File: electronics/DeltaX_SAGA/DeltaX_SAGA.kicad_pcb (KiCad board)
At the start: 4 copper layers, 51.2 x 58.9 mm, 68 parts, among them J1 USB_B_Micro, J10 Motor3_Encoder, J11 Motor1_OUT, J12 Motor2_OUT, J13 Motor3_OUT, J14 TestPt1, J15 TestPt2, J16 TestGND, J18 STLink, J2 Programmer, J3 Servo Signal, J4 Servo Power, J5 Power(6-38V), J6 Thrower Signal, J7 Thrower Power, J8 Motor1_Encoder, J9 Motor2_Encoder, U1 CM1223, U10 DRV8243, U11 DRV8243, U2 NCP164C, U3 STM32G441KB, U4 NCV8730, U5 NCP164C, U6 MAX14930, U7 MAX14930, U8 MAX12930, U9 DRV8243

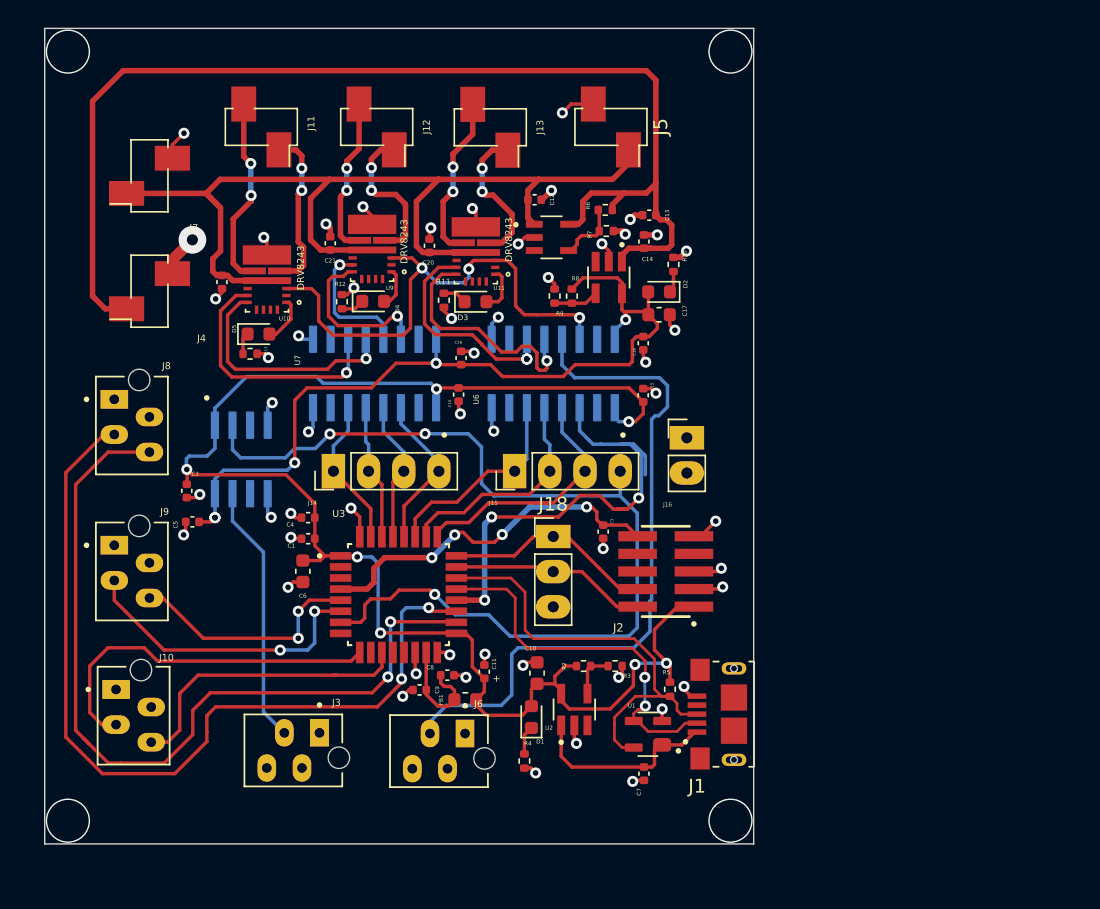
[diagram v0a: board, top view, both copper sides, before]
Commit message: Updated the PCB design
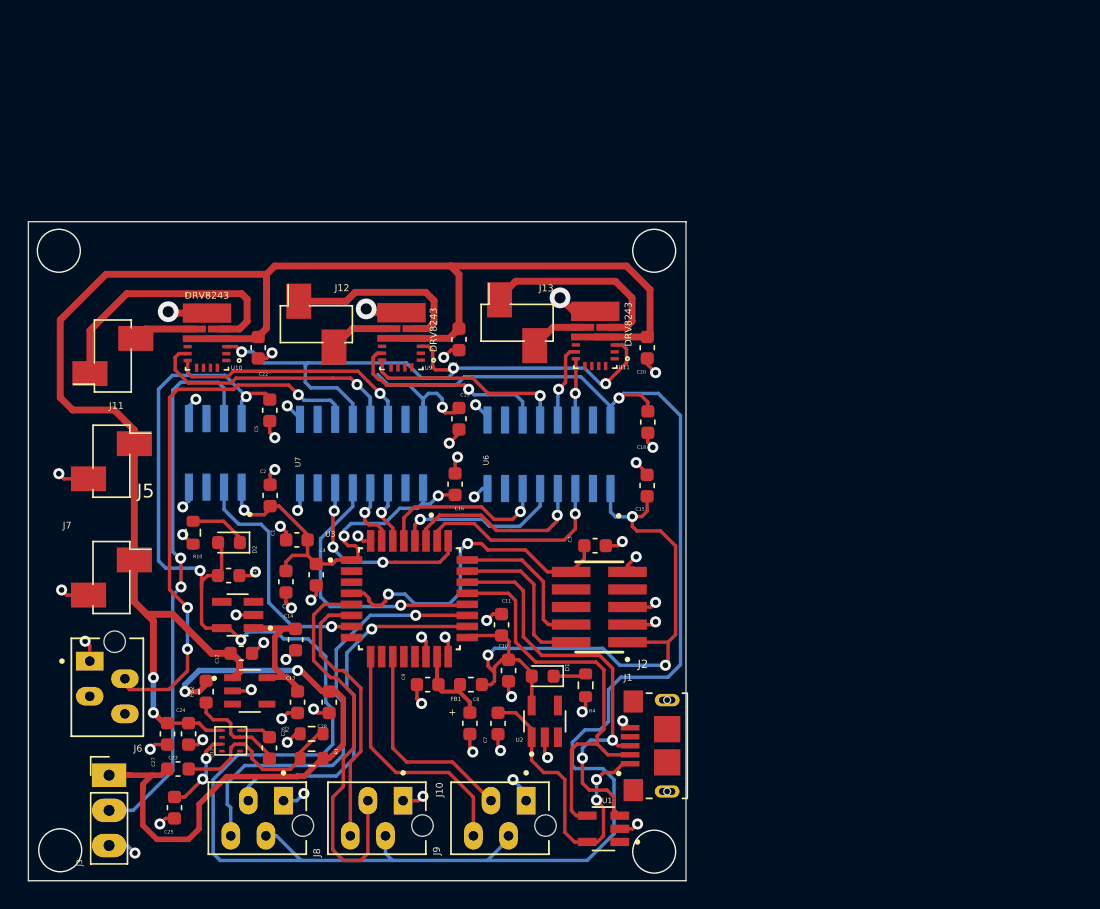
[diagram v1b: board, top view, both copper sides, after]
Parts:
- removed D3, D4, D5: LED, LED_SMD:LED_0603_1608Metric
- removed J14: TestPt1, Connector_PinHeader_2.54mm:PinHeader_1x04_P2.54mm_Vertical
- removed J15: TestPt2, Connector_PinHeader_2.54mm:PinHeader_1x04_P2.54mm_Vertical
- removed J16: TestGND, Connector_PinHeader_2.54mm:PinHeader_1x02_P2.54mm_Vertical
- removed J18: STLink, Connector_PinHeader_2.54mm:PinHeader_1x03_P2.54mm_Vertical
- removed J4: Servo Power, Connector_PinHeader_2.54mm:PinHeader_1x02_P2.54mm_Vertical_SMD_Pin1Right
- removed R11, R12, R13, R5: 1k5, Resistor_SMD:R_0402_1005Metric
- removed R3: 100k, Resistor_SMD:R_0402_1005Metric
- removed R6: 2M4, Resistor_SMD:R_0402_1005Metric
- removed R7: 750k, Resistor_SMD:R_0402_1005Metric
- removed R8: R1, Resistor_SMD:R_0402_1005Metric
- removed R9: R2, Resistor_SMD:R_0402_1005Metric
- added C23: 10uF, Capacitor_SMD:C_0603_1608Metric, F.Cu at (110.7, 123.2)
- added C24: 100nF, Capacitor_SMD:C_0603_1608Metric, F.Cu at (112.3, 123.2)
- added C25: 33nF, Capacitor_SMD:C_0603_1608Metric, F.Cu at (111.3, 128.5)
- added C26: 100nF, Capacitor_SMD:C_0603_1608Metric, F.Cu at (118.1, 124.2)
- added C27: 22pF, Capacitor_SMD:C_0603_1608Metric, F.Cu at (111.5, 125.7)
- added C28: 47uF, Capacitor_SMD:C_0603_1608Metric, F.Cu at (122.4, 120.9)
- added FB2: FerriteBead_Small, Inductor_SMD:L_0603_1608Metric, F.Cu at (113.5, 120.1)
- added R1: 52k3, Resistor_SMD:R_0603_1608Metric, F.Cu at (121.2, 125.0)
- added U12: TPS62932, TPS62933:TPS62933, F.Cu at (114.7, 122.9)
- C1, C11, C12, C13, C14, C15, C16, C18, C19, C2, C3, C4, C5, C7, C8, C9: footprint Capacitor_SMD:C_0402_1005Metric -> Capacitor_SMD:C_0603_1608Metric
- C20, C21, C22: value 0.1uF -> 50uF; footprint Capacitor_SMD:C_0402_1005Metric -> Capacitor_SMD:C_0603_1608Metric
- J3: value Servo Signal -> SERVO; footprint Micro-MaTch215079-4:TE_7-215079-4 -> Connector_PinHeader_2.54mm:PinHeader_1x03_P2.54mm_Vertical
- R10, R4: footprint Resistor_SMD:R_0402_1005Metric -> Resistor_SMD:R_0603_1608Metric
- R2: value 200k -> 10k; footprint Resistor_SMD:R_0402_1005Metric -> Resistor_SMD:R_0603_1608Metric
- U1: footprint CM1223:SOT192P237X122-4N -> CM1223-02SO:SOT95P280X145-5N
- moved J5 43.4 mm to (106.7, 103.5), turned to 0 degrees
- moved C13 43.4 mm to (120.1, 120.9), turned to -90 degrees
- moved R10 39.7 mm to (112.6, 108.7), turned to -90 degrees
- moved U4 39.3 mm to (116.7, 120.1)
- moved C12 39.0 mm to (116.1, 117.4)
- moved C14 38.2 mm to (120.0, 116.4), turned to -90 degrees
- moved C17 36.4 mm to (115.2, 111.8)
- moved U5 36.2 mm to (115.8, 114.6), turned to 180 degrees
- moved D2 36.0 mm to (115.2, 109.4)
- moved J8 31.5 mm to (119.1, 128.0), turned to 0 degrees
- moved J10 30.7 mm to (136.7, 128.0), turned to 0 degrees
- moved J7 29.1 mm to (106.7, 111.9), turned to 0 degrees
- moved J9 27.8 mm to (127.8, 128.0), turned to 0 degrees
- moved J6 27.6 mm to (105.1, 117.9), turned to 90 degrees
- moved R2 20.2 mm to (121.2, 123.2), turned to 180 degrees
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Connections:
- J10 pad 1: unconnected-(J10-Pad1) -> GND2
- J10 pad 2: GND2 -> /3V3
- J10 pad 3: /Motor3_ENCB -> /Motor3_ENCA
- J10 pad 4: /Motor3_ENCA -> /Motor3_ENCB
- J3 pad 1: unconnected-(J3-Pad1) -> /5V_OUT
- J3 pad 2: GND2 -> /Servo_PWM_Isolated
- J3 pad 3: /Servo_PWM_Isolated -> GND2
- J6 pad 1: unconnected-(J6-Pad1) -> GND2
- J6 pad 2: GND2 -> /Thrower_PWM_Isolated
- J6 pad 3: /Thrower_PWM_Isolated -> unconnected-(J6-Pad3)
- J8 pad 1: unconnected-(J8-Pad1) -> GND2
- J8 pad 2: GND2 -> /3V3
- J8 pad 3: /Motor1_ENCB -> /Motor1_ENCA
- J8 pad 4: /Motor1_ENCA -> /Motor1_ENCB
- J9 pad 1: unconnected-(J9-Pad1) -> GND2
- J9 pad 2: GND2 -> /3V3
- J9 pad 3: /Motor2_ENCB -> /Motor2_ENCA
- J9 pad 4: /Motor2_ENCA -> /Motor2_ENCB
- R2 pad 1: /3.3V -> Net-(C27-Pad2)
- R2 pad 2: Net-(R2-Pad2) -> GND2
- U1 pad 1: +5V -> unconnected-(U1-Pad1)
- U1 pad 3: /USB_D- -> /USB_D+
- U1 pad 4: /USB_D+ -> /USB_D-
- U10 pad 1: /nFAULT1 -> unconnected-(U10-Pad1)
- U11 pad 1: /nFAULT3 -> unconnected-(U11-Pad1)
- U2 pad 4: Net-(R2-Pad2) -> unconnected-(U2-Pad4)
- U4 pad 4: Net-(R6-Pad2) -> unconnected-(U4-Pad4)
- U5 pad 4: Net-(R8-Pad2) -> unconnected-(U5-Pad4)
- U6 pad 11: /Motor3_PWM_Isolated -> /Motor2_PWM_Isolated
- U6 pad 12: /Motor3_DIR_Isolated -> /Motor2_DIR_Isolated
- U6 pad 13: /Thrower_PWM_Isolated -> /Motor3_PWM_Isolated
- U6 pad 14: /nSLEEP_Isolated -> /Motor3_DIR_Isolated
- U6 pad 3: /nSLEEP -> /Motor3_DIR
- U6 pad 4: /Thrower_PWM -> /Motor3_PWM
- U6 pad 5: /Motor3_DIR -> /Motor2_DIR
- U6 pad 6: /Motor3_PWM -> /Motor2_PWM
- U7 pad 11: /Motor1_PWM_Isolated -> /Thrower_PWM_Isolated
- U7 pad 12: /Motor1_DIR_Isolated -> /nSLEEP_Isolated
- U7 pad 13: /Motor2_PWM_Isolated -> /Motor1_PWM_Isolated
- U7 pad 14: /Motor2_DIR_Isolated -> /Motor1_DIR_Isolated
- U7 pad 3: /Motor2_DIR -> /Motor1_DIR
- U7 pad 4: /Motor2_PWM -> /Motor1_PWM
- U7 pad 5: /Motor1_DIR -> /nSLEEP
- U7 pad 6: /Motor1_PWM -> /Thrower_PWM
- U9 pad 1: /nFAULT2 -> unconnected-(U9-Pad1)
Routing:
- net /3V3: track 60.0 -> 180.7 mm
- net +5VA: track 85.6 -> 11.3 mm
- net /Servo_PWM: track 70.6 -> 17.3 mm, vias 3 -> 1
- net /5V_OUT: track 0.00 -> 48.8 mm, vias 0 -> 2
- net /V+: track 73.1 -> 118.1 mm, vias 0 -> 2
- net /Motor1_ENCA: track 60.5 -> 26.8 mm, vias 2 -> 1
- net /3.3V: track 112.3 -> 78.6 mm, vias 7 -> 6
- net /Motor1_ENCB: track 62.2 -> 31.5 mm, vias 2 -> 1
- net /Servo_PWM_Isolated: track 18.8 -> 40.1 mm, vias 0 -> 2
- net /nSLEEP: track 34.5 -> 19.8 mm, vias 3 -> 1
- net Net-(C27-Pad2): track 0.00 -> 13.3 mm
- net /Motor3_DIR_Isolated: track 17.7 -> 4.44 mm
- net GND2: track 36.5 -> 48.6 mm, vias 27 -> 31
- net /Motor2_ENCA: track 17.3 -> 29.0 mm, vias 2 -> 0
- net /Motor3_PWM_Isolated: track 15.7 -> 5.72 mm, vias 2 -> 1
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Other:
- board size 51.2 x 58.9 mm -> 47.5 x 47.6 mm

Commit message: Updated the PCB design
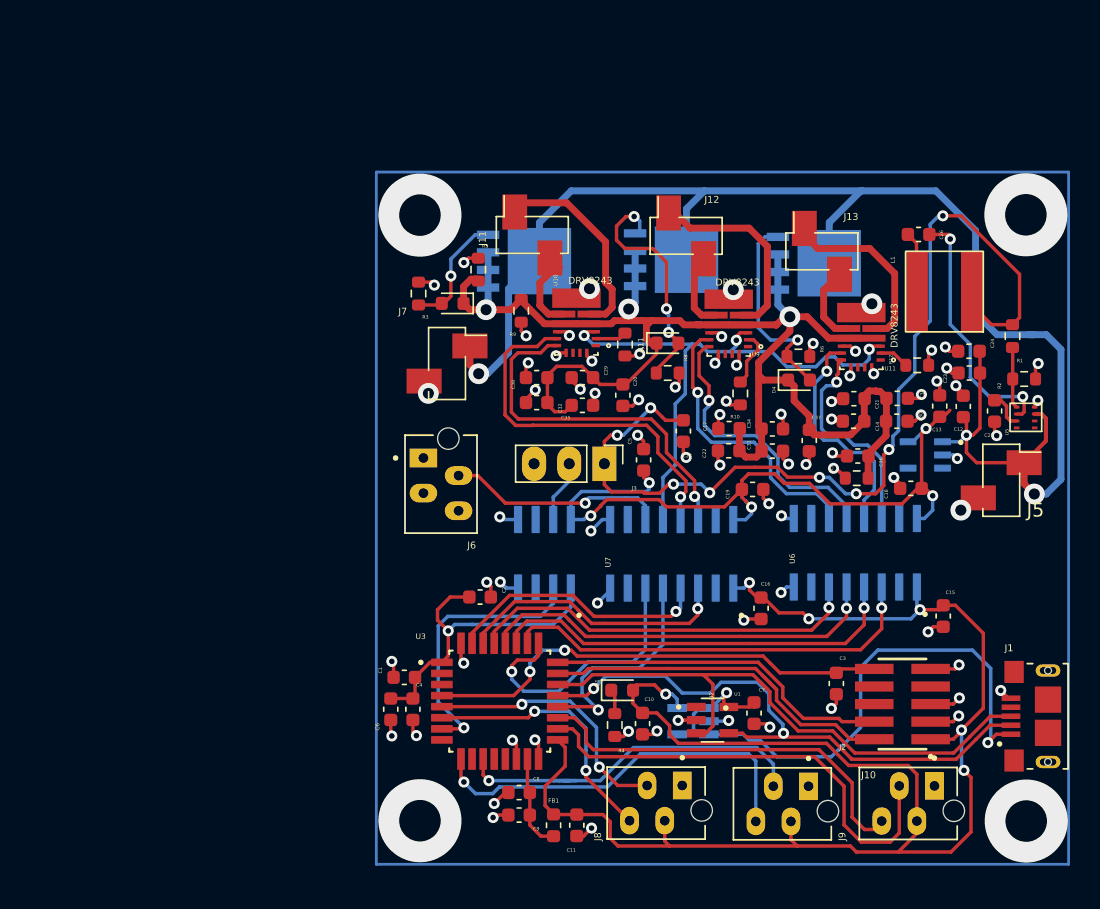
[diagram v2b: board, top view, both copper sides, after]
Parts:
- removed C28: 47uF, Capacitor_SMD:C_0603_1608Metric
- removed D2: LED, LED_SMD:LED_0603_1608Metric
- removed FB2: FerriteBead_Small, Inductor_SMD:L_0603_1608Metric
- removed U12: TPS62932, TPS62933:TPS62933
- added C29: 10uF, Capacitor_SMD:C_0603_1608Metric, F.Cu at (140.7, 97.5)
- added C30: 10uF, Capacitor_SMD:C_0603_1608Metric, F.Cu at (163.4, 100.6)
- added C31: 10uF, Capacitor_SMD:C_0603_1608Metric, F.Cu at (154.4, 102.8)
- added C32: 10uF, Capacitor_SMD:C_0603_1608Metric, F.Cu at (137.4, 99.3)
- added C33: 10uF, Capacitor_SMD:C_0603_1608Metric, F.Cu at (163.4, 99.0)
- added C34: 10uF, Capacitor_SMD:C_0603_1608Metric, F.Cu at (154.4, 101.2)
- added C35: 10uF, Capacitor_SMD:C_0603_1608Metric, F.Cu at (140.7, 99.5)
- added C36: 10uF, Capacitor_SMD:C_0603_1608Metric, F.Cu at (160.6, 103.1)
- added C37: 10uF, Capacitor_SMD:C_0603_1608Metric, F.Cu at (157.1, 102.0)
- added C38: 10uF, Capacitor_SMD:C_0603_1608Metric, F.Cu at (137.4, 97.5)
- added D3: 1N53xxB, Diode_SMD:D_0603_1608Metric, F.Cu at (131.3, 92.1)
- added D4: 1N53xxB, Diode_SMD:D_0603_1608Metric, F.Cu at (156.4, 97.6)
- added D5: 1N53xxB, Diode_SMD:D_0603_1608Metric, F.Cu at (146.9, 95.0)
- added L1: 7.6uH, SRP6060FA5R6M:SRP6060FA5R6M, F.Cu at (170.2, 94.4)
- added Q1: BUK6Y10, BUK6Y10:TO127P600X120-5N, F.Cu at (136.6, 88.5)
- added Q2: BUK6Y10, BUK6Y10:TO127P600X120-5N, F.Cu at (157.5, 88.3)
- added Q3: BUK6Y10, BUK6Y10:TO127P600X120-5N, F.Cu at (147.2, 88.2)
- added R11: 3k, Resistor_SMD:R_0603_1608Metric, F.Cu at (143.8, 95.1)
- added R12: 3k, Resistor_SMD:R_0603_1608Metric, F.Cu at (164.9, 96.6)
- added R3: 100, Resistor_SMD:R_0603_1608Metric, F.Cu at (128.9, 91.4)
- added R5: 10, Resistor_SMD:R_0603_1608Metric, F.Cu at (133.2, 89.7)
- added R6: 100, Resistor_SMD:R_0603_1608Metric, F.Cu at (156.3, 95.9)
- added R7: 10, Resistor_SMD:R_0603_1608Metric, F.Cu at (160.5, 104.7)
- added R8: 100, Resistor_SMD:R_0603_1608Metric, F.Cu at (146.9, 97.1)
- added R9: 10, Resistor_SMD:R_0603_1608Metric, F.Cu at (136.3, 92.6)
- C14: value 1uF -> 10uF
- C20, C21, C22: value 50uF -> 10uF
- C27: value 22pF -> 100uF
- R10: value 1k5 -> 3k
- U5: value NCP164C -> TPS62933; footprint NCP164C:SOP95P275X110-5N -> TPS62933:TPS62933
- moved C25 65.8 mm to (170.5, 99.9)
- moved J5 64.3 mm to (171.0, 104.9)
- moved C23 63.5 mm to (168.7, 97.1), turned to 180 degrees
- moved C24 62.8 mm to (168.6, 95.6), turned to 180 degrees
- moved C26 59.8 mm to (165.0, 87.1), turned to 180 degrees
- moved U5 59.1 mm to (173.4, 101.1)
- moved R1 59.1 mm to (171.8, 94.5), turned to 90 degrees
- moved R2 57.5 mm to (172.6, 97.6)
- moved C12 55.1 mm to (168.2, 99.5), turned to 90 degrees
- moved U4 51.7 mm to (165.5, 103.0)
- moved C13 51.1 mm to (166.5, 99.5), turned to 90 degrees
- moved C27 43.9 mm to (148.0, 101.3), turned to 90 degrees
- moved C14 43.3 mm to (160.3, 100.6), turned to 180 degrees
- moved J3 42.3 mm to (142.3, 103.7), turned to -90 degrees
- moved R10 40.8 mm to (152.1, 98.6), turned to 90 degrees
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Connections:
- C1 pad 1: /3.3V -> +3.3V
- C10 pad 1: /3.3V -> +3.3V
- C11 pad 1: /3.3V -> +3.3V
- C14 pad 1: +5VA -> /VM
- C15 pad 2: /3.3V -> +3.3V
- C16 pad 2: /3.3V -> +3.3V
- C17 pad 1: /3V3 -> /VM
- C18 pad 2: /3V3 -> +5VA
- C19 pad 2: /3V3 -> +5VA
- C2 pad 2: /3.3V -> +3.3V
- C20 pad 1: /V+ -> /VM
- C21 pad 1: /V+ -> /VM
- C22 pad 1: /V+ -> /VM
- C27 pad 1: /5V_OUT -> GND2
- C27 pad 2: Net-(C27-Pad2) -> +5VD
- C4 pad 1: /3.3V -> +3.3V
- C5 pad 1: /3V3 -> +5VA
- C6 pad 1: /3.3V -> +3.3V
- D1 pad 2: /3.3V -> +3.3V
- FB1 pad 2: /3.3V -> +3.3V
- J10 pad 1: GND2 -> GND
- J10 pad 2: /3V3 -> +3.3V
- J2 pad 1: /3.3V -> +3.3V
- J3 pad 1: /5V_OUT -> +5VD
- J8 pad 1: GND2 -> GND
- J8 pad 2: /3V3 -> +3.3V
- J9 pad 1: GND2 -> GND
- J9 pad 2: /3V3 -> +3.3V
- R1 pad 1: /5V_OUT -> Net-(R1-Pad1)
- R1 pad 2: Net-(C27-Pad2) -> +5VD
- R10 pad 1: Net-(D2-Pad1) -> GND2
- R10 pad 2: GND2 -> Net-(R10-Pad2)
- R2 pad 1: Net-(C27-Pad2) -> GND2
- R2 pad 2: GND2 -> Net-(R1-Pad1)
- U10 pad 11: unconnected-(U10-Pad11) -> GND2
- U10 pad 14: unconnected-(U10-Pad14) -> GND2
- U10 pad 2: unconnected-(U10-Pad2) -> Net-(R11-Pad2)
- U10 pad 4: /V+ -> /VM
- U10 pad 8: unconnected-(U10-Pad8) -> GND2
- U11 pad 11: unconnected-(U11-Pad11) -> GND2
- U11 pad 14: unconnected-(U11-Pad14) -> GND2
- U11 pad 2: unconnected-(U11-Pad2) -> Net-(R12-Pad2)
- U11 pad 4: /V+ -> /VM
- U11 pad 8: unconnected-(U11-Pad8) -> GND2
- U2 pad 3: unconnected-(U2-Pad3) -> +5V
- U2 pad 5: /3.3V -> +3.3V
- U3 pad 1: /3.3V -> +3.3V
- U3 pad 11: /Motor3_ENCA -> /Motor2_ENCA
- U3 pad 17: /3.3V -> +3.3V
- U3 pad 18: /Motor1_ENCA -> /Motor3_ENCA
- U3 pad 19: /Motor1_ENCB -> /Motor3_ENCB
- U3 pad 5: /Motor2_ENCA -> /Motor1_ENCA
- U3 pad 6: /Motor2_ENCB -> /Motor1_ENCB
- U3 pad 9: /Motor3_ENCB -> /Motor2_ENCB
- U5 pad 1: +5VA -> unconnected-(U5-Pad1)
- U5 pad 2: GND2 -> unconnected-(U5-Pad2)
- U5 pad 3: unconnected-(U5-Pad3) -> /V+
- U5 pad 4: unconnected-(U5-Pad4) -> GND2
- U5 pad 5: /3V3 -> Net-(R1-Pad1)
- U6 pad 1: /3.3V -> +3.3V
- U6 pad 16: /3V3 -> +5VA
- U7 pad 1: /3.3V -> +3.3V
- U7 pad 16: /3V3 -> +5VA
- U8 pad 1: /3.3V -> +3.3V
- U8 pad 8: /3V3 -> +5VA
- U9 pad 11: unconnected-(U9-Pad11) -> GND2
- U9 pad 14: unconnected-(U9-Pad14) -> GND2
- U9 pad 2: unconnected-(U9-Pad2) -> Net-(R10-Pad2)
- U9 pad 4: /V+ -> /VM
- U9 pad 8: unconnected-(U9-Pad8) -> GND2
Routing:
- net /3V3: track 180.7 -> 0.00 mm, vias 5 -> 0
- net +3.3V: track 0.00 -> 142.6 mm, vias 0 -> 7
- net /VM: track 0.00 -> 101.6 mm, vias 0 -> 3
- net /3.3V: track 78.6 -> 0.00 mm, vias 6 -> 0
- net +5VD: track 0.00 -> 70.7 mm, vias 0 -> 9
- net /5V_OUT: track 48.8 -> 0.00 mm, vias 2 -> 0
- net +5VA: track 11.3 -> 54.3 mm, vias 0 -> 5
- net /Servo_PWM_Isolated: track 40.1 -> 4.51 mm, vias 2 -> 0
- net /Thrower_PWM_Isolated: track 39.9 -> 15.8 mm, vias 3 -> 1
- net +5V: track 22.4 -> 43.6 mm
- net /Motor3_ENCA: track 15.3 -> 33.9 mm
- net Net-(D5-Pad2): track 0.00 -> 17.5 mm, vias 0 -> 3
- net /Motor2_DIR: track 12.5 -> 29.4 mm
- net /Motor3_PWM: track 13.9 -> 30.2 mm
- net Net-(C26-Pad1): track 2.33 -> 18.5 mm, vias 0 -> 2
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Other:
- board outline removed
- rule pad_to_mask_clearance: 0 -> 0.25
- board text removed: "+"

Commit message: complete PCB updated
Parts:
- removed D3, D4, D5: 1N53xxB, Diode_SMD:D_0603_1608Metric
- removed Q2, Q3: BUK6Y10, BUK6Y10:TO127P600X120-5N
- removed R5, R7, R9: 10, Resistor_SMD:R_0603_1608Metric
- removed R6, R8: 100, Resistor_SMD:R_0603_1608Metric
- added J14: M31, 1pinSMD:1PinSMD, F.Cu at (154.5, 85.6)
- added J15: M33, 1pinSMD:1PinSMD, F.Cu at (157.0, 85.6)
- added J16: Thrower+, 1pinSMD:1PinSMD, F.Cu at (129.3, 99.1)
- added J17: Thrower-, 1pinSMD:1PinSMD, F.Cu at (129.3, 96.5)
- added J4: M11, 1pinSMD:1PinSMD, F.Cu at (136.8, 86.0)
- C10: footprint Capacitor_SMD:C_0603_1608Metric -> Capacitor_SMD:C_0805_2012Metric
- C12, C13, C18, C19, C24, C25, C26, C27, C5, Q1, R1, R10, R11, R12, R2, R3, U4: moved to B.Cu
- C14, C17, C20, C21, C22, C23, C29, C30, C31, C32, C33, C34, C35, C36, C37, C38: footprint Capacitor_SMD:C_0603_1608Metric -> Capacitor_SMD:C_0805_2012Metric; moved to B.Cu
- J11: value Motor1_OUT -> M12; footprint Connector_PinHeader_2.54mm:PinHeader_1x02_P2.54mm_Vertical_SMD_Pin1Right -> 1pinSMD:1PinSMD
- J12: value Motor2_OUT -> M21; footprint Connector_PinHeader_2.54mm:PinHeader_1x02_P2.54mm_Vertical_SMD_Pin1Right -> 1pinSMD:1PinSMD
- J13: value Motor3_OUT -> M22; footprint Connector_PinHeader_2.54mm:PinHeader_1x02_P2.54mm_Vertical_SMD_Pin1Right -> 1pinSMD:1PinSMD
- J5: value Power(6-38V) -> Battery+; footprint Connector_PinHeader_2.54mm:PinHeader_1x02_P2.54mm_Vertical_SMD_Pin1Right -> 1pinSMD:1PinSMD
- J7: value Thrower Power -> Battery-; footprint Connector_PinHeader_2.54mm:PinHeader_1x02_P2.54mm_Vertical_SMD_Pin1Right -> 1pinSMD:1PinSMD
- moved J7 41.7 mm to (172.7, 95.5)
- moved R3 34.4 mm to (163.3, 90.3), turned to -90 degrees
- moved Q1 27.0 mm to (163.5, 88.1), turned to 90 degrees
- moved C26 20.5 mm to (151.7, 102.7), turned to 90 degrees
- moved U5 20.3 mm to (153.1, 100.0)
- moved L1 19.9 mm to (150.6, 98.2), turned to 180 degrees
- moved R1 17.6 mm to (154.9, 99.3)
- moved C25 17.4 mm to (153.4, 103.0)
- moved R2 16.1 mm to (156.6, 99.3), turned to 90 degrees
- moved J5 12.5 mm to (172.7, 92.5)
- moved C13 11.4 mm to (155.7, 102.8)
- moved J13 11.2 mm to (147.1, 85.7)
- moved C36 9.86 mm to (167.3, 95.8), turned to -90 degrees
- moved C20 9.06 mm to (135.1, 95.6)
- moved C12 8.42 mm to (159.8, 99.1), turned to 180 degrees
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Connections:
- J12 pad 1: /Motor2_OUT2 -> /Motor2_OUT1
- J13 pad 1: /Motor3_OUT2 -> /Motor2_OUT2
- J7 pad 1: /V+ -> GND2
- L1 pad 1: Net-(C26-Pad2) -> Net-(C26-Pad1)
- R1 pad 1: Net-(R1-Pad1) -> +5VD
- R1 pad 2: +5VD -> /FB
- R2 pad 2: Net-(R1-Pad1) -> /FB
- U5 pad 5: Net-(R1-Pad1) -> Net-(C26-Pad2)
- U5 pad 8: unconnected-(U5-Pad8) -> /FB
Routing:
- net +5VD: track 70.7 -> 32.4 mm, vias 9 -> 2
- net GND2: track 59.5 -> 21.1 mm, vias 53 -> 48
- net /VM: track 101.6 -> 67.1 mm, vias 3 -> 1
- net Net-(D5-Pad2): track 17.5 -> 0.00 mm, vias 3 -> 0
- net +5VA: track 54.3 -> 37.0 mm, vias 5 -> 3
- net GND: track 35.6 -> 20.1 mm
- net Net-(D4-Pad2): track 14.9 -> 0.00 mm, vias 1 -> 0
- net /V+: track 110.3 -> 97.7 mm
- net /Motor1_OUT2: track 14.8 -> 5.65 mm
- net /Motor2_OUT2: track 14.6 -> 5.98 mm
- net /Motor3_DIR_Isolated: track 15.8 -> 23.4 mm
- net /Motor3_OUT2: track 13.3 -> 5.92 mm
- net /Motor3_PWM_Isolated: track 17.3 -> 24.6 mm
- net Net-(C26-Pad1): track 18.5 -> 11.4 mm, vias 2 -> 1
- net /Motor2_PWM_Isolated: track 20.9 -> 27.9 mm
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- added copper zone on In2.Cu, net GND
- added copper zone on In1.Cu, net GND2
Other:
- rule pad_to_mask_clearance: 0.25 -> 0.05

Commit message: complete PCB updated
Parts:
- Q1: moved to F.Cu
- moved R3 3.39 mm to (163.5, 87.0)
- moved Q1 1.50 mm to (164.0, 86.7), turned to -90 degrees
- moved J6 0.36 mm to (129.2, 103.6)
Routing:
- net /nSLEEP_Isolated: track 41.8 -> 38.8 mm
- net Net-(Q1-Pad4): track 3.47 -> 6.17 mm
- net /Thrower_PWM_Isolated: track 15.4 -> 13.3 mm
- net /V+: track 97.7 -> 98.3 mm
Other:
- board outline added: 50 x 50 mm
